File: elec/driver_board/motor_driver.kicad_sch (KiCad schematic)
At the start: 9 parts, among them U19 74HCT595, U20 VID6606

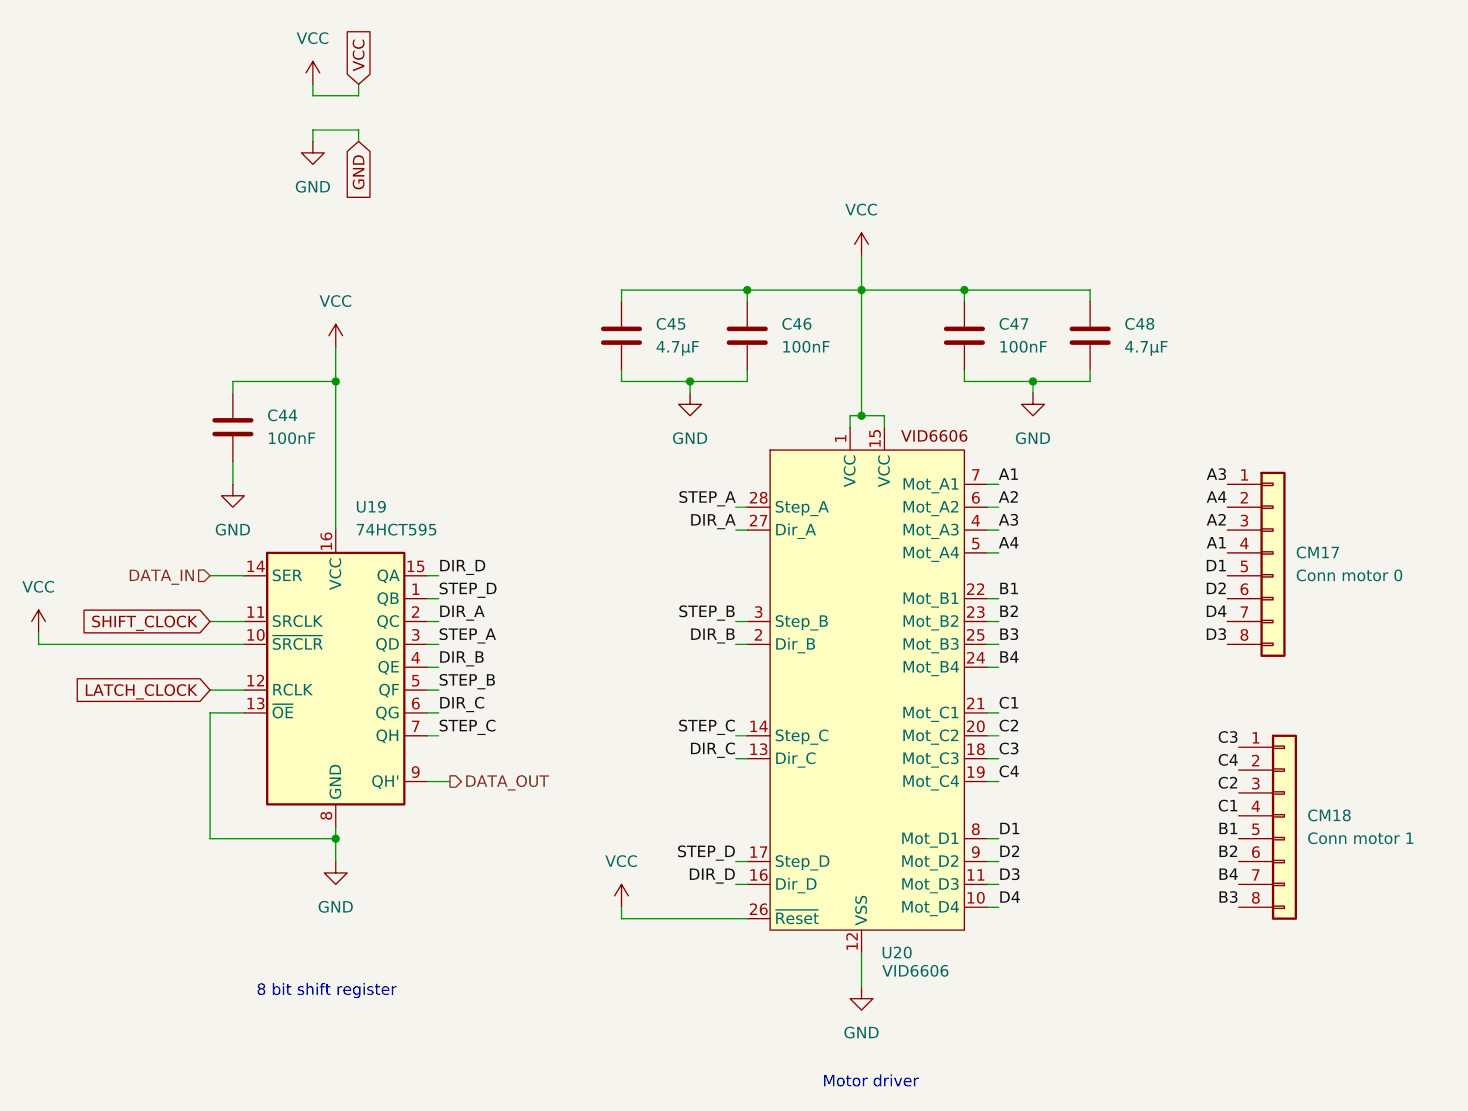
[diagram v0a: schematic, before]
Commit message: Update footprint of the level shifter
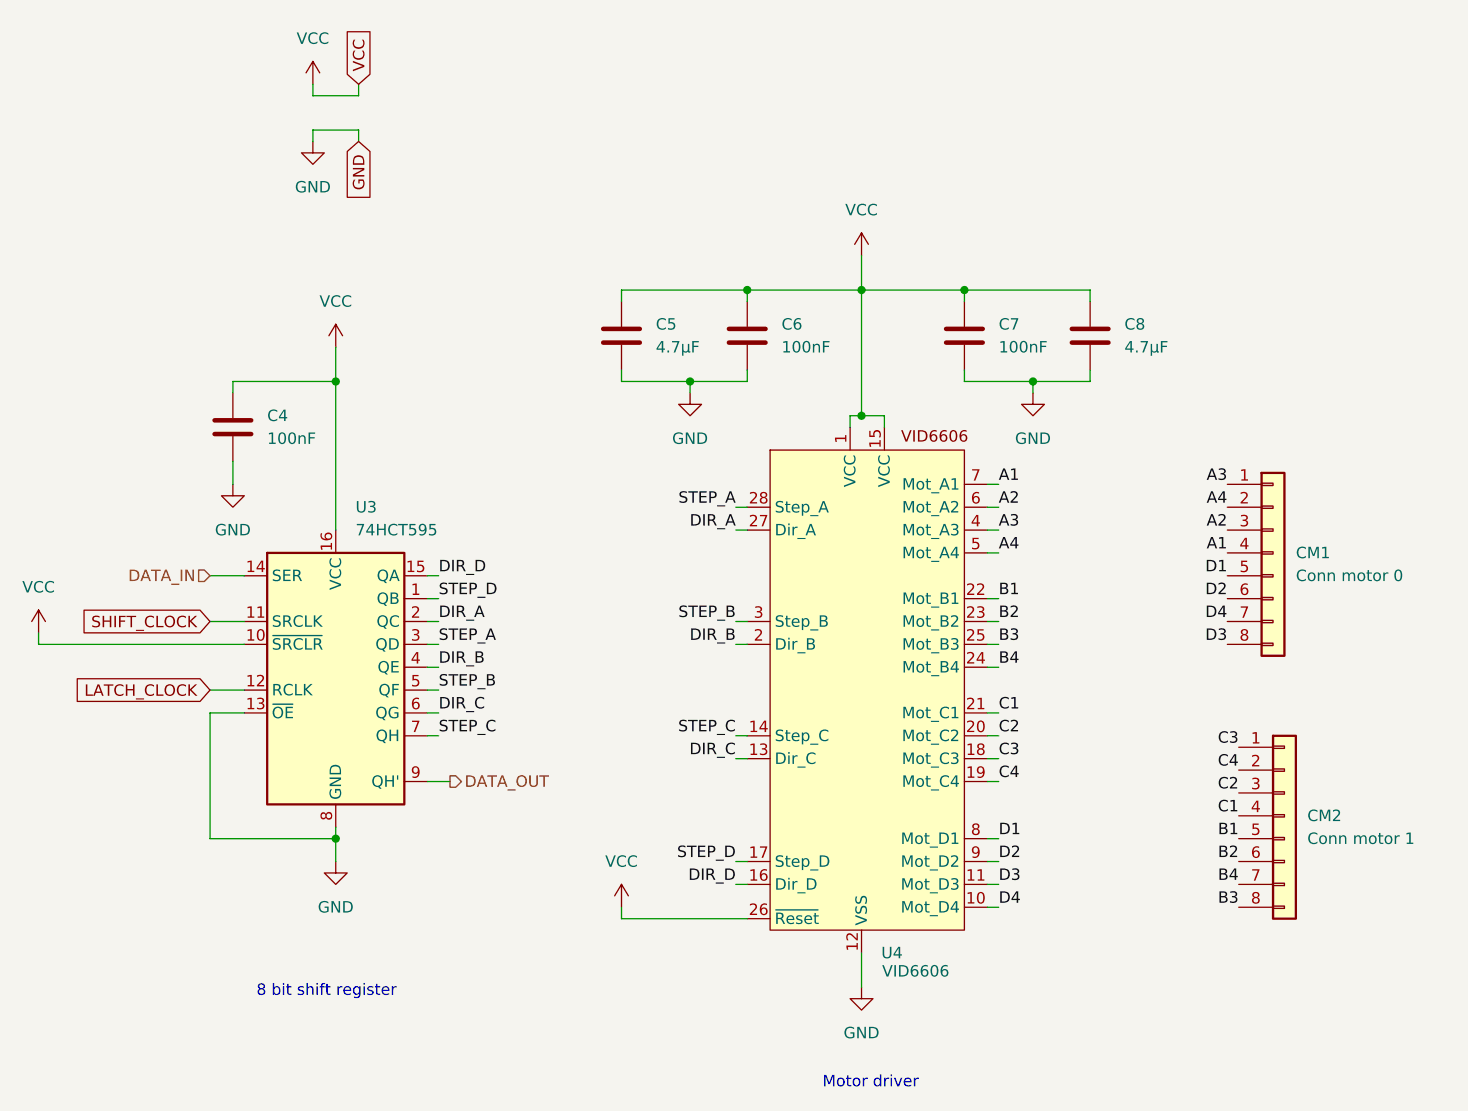
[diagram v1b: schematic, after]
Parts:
- renumbered C44 to C4, C45 to C5, C46 to C6, C47 to C7, C48 to C8, CM17 to CM1, CM18 to CM2, U19 to U3, U20 to U4
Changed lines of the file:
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@@
 (kicad_sch
-	(version 20231120)
+	(version 20250114)
 	(generator "eeschema")
-	(generator_version "8.0")
+	(generator_version "9.0")
 	(paper "A4")
 	(title_block
@@
 		(rev "2")
 	)
+	(text "8 bit shift register"
+		(exclude_from_sim no)
+		(at 104.394 141.478 0)
+		(effects
+			(font
+				(size 1.27 1.27)
+			)
+		)
+	)
+	(text "Motor driver"
+		(exclude_from_sim no)
+		(at 164.846 151.638 0)
+		(effects
+			(font
+				(size 1.27 1.27)
+			)
+		)
+	)
 	(junction
 		(at 144.78 73.66)
@@
 		)
 	)
-	(text "8 bit shift register"
-		(exclude_from_sim no)
-		(at 104.394 141.478 0)
-		(effects
-			(font
-				(size 1.27 1.27)
-			)
-		)
-	)
-	(text "Motor driver"
-		(exclude_from_sim no)
-		(at 164.846 151.638 0)
-		(effects
-			(font
-				(size 1.27 1.27)
-			)
-		)
-	)
 	(label "DIR_B"
 		(at 116.84 105.41 0)
@@
 		(dnp no)
 		(fields_autoplaced yes)
-		(property "Reference" "#PWR0106"
+		(property "Reference" "#PWR018"
 			(at 105.41 133.35 0)
 			(effects
@@
 		(dnp no)
 		(fields_autoplaced yes)
-		(property "Reference" "#PWR0111"
+		(property "Reference" "#PWR023"
 			(at 182.88 81.28 0)
 			(effects
@@
 		(dnp no)
 		(fields_autoplaced yes)
-		(property "Reference" "C44"
+		(property "Reference" "C4"
 			(at 97.79 77.4699 0)
 			(effects
@@
 		(dnp no)
 		(fields_autoplaced yes)
-		(property "Reference" "U19"
+		(property "Reference" "U3"
 			(at 107.6041 87.63 0)
 			(effects
@@
 		(dnp no)
 		(fields_autoplaced yes)
-		(property "Reference" "C46"
+		(property "Reference" "C6"
 			(at 154.94 67.3099 0)
 			(effects
@@
 		(dnp no)
 		(fields_autoplaced yes)
-		(property "Reference" "#PWR0102"
+		(property "Reference" "#PWR014"
 			(at 93.98 91.44 0)
 			(effects
@@
 		(dnp no)
 		(fields_autoplaced yes)
-		(property "Reference" "#PWR0104"
+		(property "Reference" "#PWR016"
 			(at 102.87 53.34 0)
 			(effects
@@
 		(dnp no)
 		(fields_autoplaced yes)
-		(property "Reference" "#PWR0105"
+		(property "Reference" "#PWR017"
 			(at 105.41 73.66 0)
 			(effects
@@
 		(dnp no)
 		(fields_autoplaced yes)
-		(property "Reference" "#PWR0101"
+		(property "Reference" "#PWR013"
 			(at 72.39 105.41 0)
 			(effects
@@
 		(on_board yes)
 		(dnp no)
-		(property "Reference" "U20"
+		(property "Reference" "U4"
 			(at 166.0241 137.16 0)
 			(effects
@@
 		(dnp no)
 		(fields_autoplaced yes)
-		(property "Reference" "#PWR0107"
+		(property "Reference" "#PWR019"
 			(at 137.16 135.89 0)
 			(effects
@@
 		(on_board yes)
 		(dnp no)
-		(property "Reference" "#PWR0110"
+		(property "Reference" "#PWR022"
 			(at 163.83 147.32 0)
 			(effects
@@
 		(dnp no)
 		(fields_autoplaced yes)
-		(property "Reference" "#PWR0108"
+		(property "Reference" "#PWR020"
 			(at 144.78 81.28 0)
 			(effects
@@
 		(dnp no)
 		(fields_autoplaced yes)
-		(property "Reference" "C47"
+		(property "Reference" "C7"
 			(at 179.07 67.3099 0)
 			(effects
@@
 		(dnp no)
 		(fields_autoplaced yes)
-		(property "Reference" "C48"
+		(property "Reference" "C8"
 			(at 193.04 67.3099 0)
 			(effects
@@
 		(dnp no)
 		(fields_autoplaced yes)
-		(property "Reference" "#PWR0109"
+		(property "Reference" "#PWR021"
 			(at 163.83 63.5 0)
 			(effects
@@
 		(dnp no)
 		(fields_autoplaced yes)
-		(property "Reference" "C45"
+		(property "Reference" "C5"
 			(at 140.97 67.3099 0)
 			(effects
@@
 		(dnp no)
 		(fields_autoplaced yes)
-		(property "Reference" "CM18"
+		(property "Reference" "CM2"
 			(at 213.36 121.9199 0)
 			(effects
@@
 		(dnp no)
 		(fields_autoplaced yes)
-		(property "Reference" "CM17"
+		(property "Reference" "CM1"
 			(at 212.09 92.7099 0)
 			(effects
@@
 		(dnp no)
 		(fields_autoplaced yes)
-		(property "Reference" "#PWR0103"
+		(property "Reference" "#PWR015"
 			(at 102.87 44.45 0)
 			(effects

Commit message: Update silkscreen
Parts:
- renumbered CM1 to M1, CM2 to M2
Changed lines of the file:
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@@
 		(dnp no)
 		(fields_autoplaced yes)
-		(property "Reference" "CM2"
+		(property "Reference" "M2"
 			(at 213.36 121.9199 0)
 			(effects
@@
 			(project "driver_board"
 				(path "/f74582a2-e122-4df8-8bf1-319684e69fbe/019d0959-b2d7-40e3-bcde-64e1ae2cba0e"
-					(reference "CM18")
+					(reference "M18")
 					(unit 1)
 				)
 				(path "/f74582a2-e122-4df8-8bf1-319684e69fbe/139340e2-704b-4f11-8f36-78173d5ff297"
-					(reference "CM8")
+					(reference "M8")
 					(unit 1)
 				)
 				(path "/f74582a2-e122-4df8-8bf1-319684e69fbe/282cdb59-849b-4e51-8c8f-1fe6c219b1fb"
-					(reference "CM22")
+					(reference "M22")
 					(unit 1)
 				)
 				(path "/f74582a2-e122-4df8-8bf1-319684e69fbe/2a294713-3d44-472d-bef5-1abebc44687b"
-					(reference "CM20")
+					(reference "M20")
 					(unit 1)
 				)
 				(path "/f74582a2-e122-4df8-8bf1-319684e69fbe/3b5368a0-d7c1-49e5-b592-54e26f9ab0f3"
-					(reference "CM10")
+					(reference "M10")
 					(unit 1)
 				)
 				(path "/f74582a2-e122-4df8-8bf1-319684e69fbe/4aecfc80-b507-4e3a-9014-cbd720ff1980"
-					(reference "CM6")
+					(reference "M6")
 					(unit 1)
 				)
 				(path "/f74582a2-e122-4df8-8bf1-319684e69fbe/4e7aa681-599e-48a1-98d2-7ee6054e5f59"
-					(reference "CM24")
+					(reference "M24")
 					(unit 1)
 				)
 				(path "/f74582a2-e122-4df8-8bf1-319684e69fbe/56b777f7-590b-4db9-98ba-01b4469f76a0"
-					(reference "CM16")
+					(reference "M16")
 					(unit 1)
 				)
 				(path "/f74582a2-e122-4df8-8bf1-319684e69fbe/81b72853-db4a-435b-a101-2d4a5729a607"
-					(reference "CM2")
+					(reference "M2")
 					(unit 1)
 				)
 				(path "/f74582a2-e122-4df8-8bf1-319684e69fbe/89777332-f368-41a1-9c8f-851eab9528aa"
-					(reference "CM14")
+					(reference "M14")
 					(unit 1)
 				)
 				(path "/f74582a2-e122-4df8-8bf1-319684e69fbe/b6dbef3c-59a4-417d-9805-2b3c0886345e"
-					(reference "CM4")
+					(reference "M4")
 					(unit 1)
 				)
 				(path "/f74582a2-e122-4df8-8bf1-319684e69fbe/ebd563aa-1f82-4f6c-b14d-9a42f69511f5"
-					(reference "CM12")
+					(reference "M12")
 					(unit 1)
 				)
@@
 		(dnp no)
 		(fields_autoplaced yes)
-		(property "Reference" "CM1"
+		(property "Reference" "M1"
 			(at 212.09 92.7099 0)
 			(effects
@@
 			(project ""
 				(path "/f74582a2-e122-4df8-8bf1-319684e69fbe/019d0959-b2d7-40e3-bcde-64e1ae2cba0e"
-					(reference "CM17")
+					(reference "M17")
 					(unit 1)
 				)
 				(path "/f74582a2-e122-4df8-8bf1-319684e69fbe/139340e2-704b-4f11-8f36-78173d5ff297"
-					(reference "CM7")
+					(reference "M7")
 					(unit 1)
 				)
 				(path "/f74582a2-e122-4df8-8bf1-319684e69fbe/282cdb59-849b-4e51-8c8f-1fe6c219b1fb"
-					(reference "CM21")
+					(reference "M21")
 					(unit 1)
 				)
 				(path "/f74582a2-e122-4df8-8bf1-319684e69fbe/2a294713-3d44-472d-bef5-1abebc44687b"
-					(reference "CM19")
+					(reference "M19")
 					(unit 1)
 				)
 				(path "/f74582a2-e122-4df8-8bf1-319684e69fbe/3b5368a0-d7c1-49e5-b592-54e26f9ab0f3"
-					(reference "CM9")
+					(reference "M9")
 					(unit 1)
 				)
 				(path "/f74582a2-e122-4df8-8bf1-319684e69fbe/4aecfc80-b507-4e3a-9014-cbd720ff1980"
-					(reference "CM5")
+					(reference "M5")
 					(unit 1)
 				)
 				(path "/f74582a2-e122-4df8-8bf1-319684e69fbe/4e7aa681-599e-48a1-98d2-7ee6054e5f59"
-					(reference "CM23")
+					(reference "M23")
 					(unit 1)
 				)
 				(path "/f74582a2-e122-4df8-8bf1-319684e69fbe/56b777f7-590b-4db9-98ba-01b4469f76a0"
-					(reference "CM15")
+					(reference "M15")
 					(unit 1)
 				)
 				(path "/f74582a2-e122-4df8-8bf1-319684e69fbe/81b72853-db4a-435b-a101-2d4a5729a607"
-					(reference "CM1")
+					(reference "M1")
 					(unit 1)
 				)
 				(path "/f74582a2-e122-4df8-8bf1-319684e69fbe/89777332-f368-41a1-9c8f-851eab9528aa"
-					(reference "CM13")
+					(reference "M13")
 					(unit 1)
 				)
 				(path "/f74582a2-e122-4df8-8bf1-319684e69fbe/b6dbef3c-59a4-417d-9805-2b3c0886345e"
-					(reference "CM3")
+					(reference "M3")
 					(unit 1)
 				)
 				(path "/f74582a2-e122-4df8-8bf1-319684e69fbe/ebd563aa-1f82-4f6c-b14d-9a42f69511f5"
-					(reference "CM11")
-					(unit 1)
-				)
+					(reference "M11")
+					(unit 1)
+				)

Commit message: Update page number
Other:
- title: Motor driver -> Clockclock
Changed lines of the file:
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@@
 	(paper "A4")
 	(title_block
-		(title "Motor driver")
-		(date "2025-01-26")
-		(rev "2")
+		(title "Clockclock")
+		(date "2025-02-26")
+		(rev "3")
 	)
 	(text "8 bit shift register"
